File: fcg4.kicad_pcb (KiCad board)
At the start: 2 copper layers, 35 x 35 mm, 34 parts, among them IC1 MP9943AGQ-Z, IC2 MP9943AGQ-Z, J1 USB4105-GF-A-120, J2 SM08B-SRSS-TB, U1 STM32G473CEUx, U2 ICM-42688-P, U4 AP2112K-3.3TRG1, U5 AP2112K-1.8TRG1, Y1 ECS-240-6-37B-7KM-TR

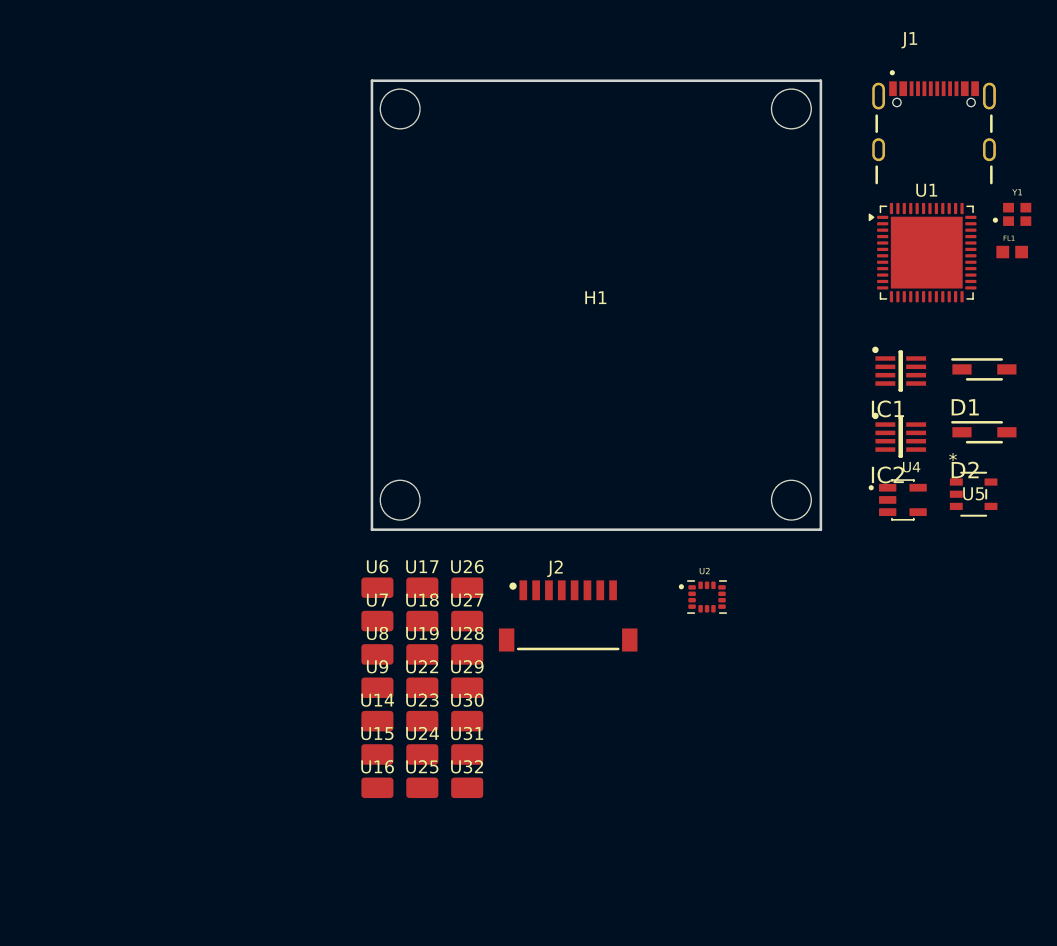
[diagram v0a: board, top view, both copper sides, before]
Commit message: - affected footprints for components - started placing components
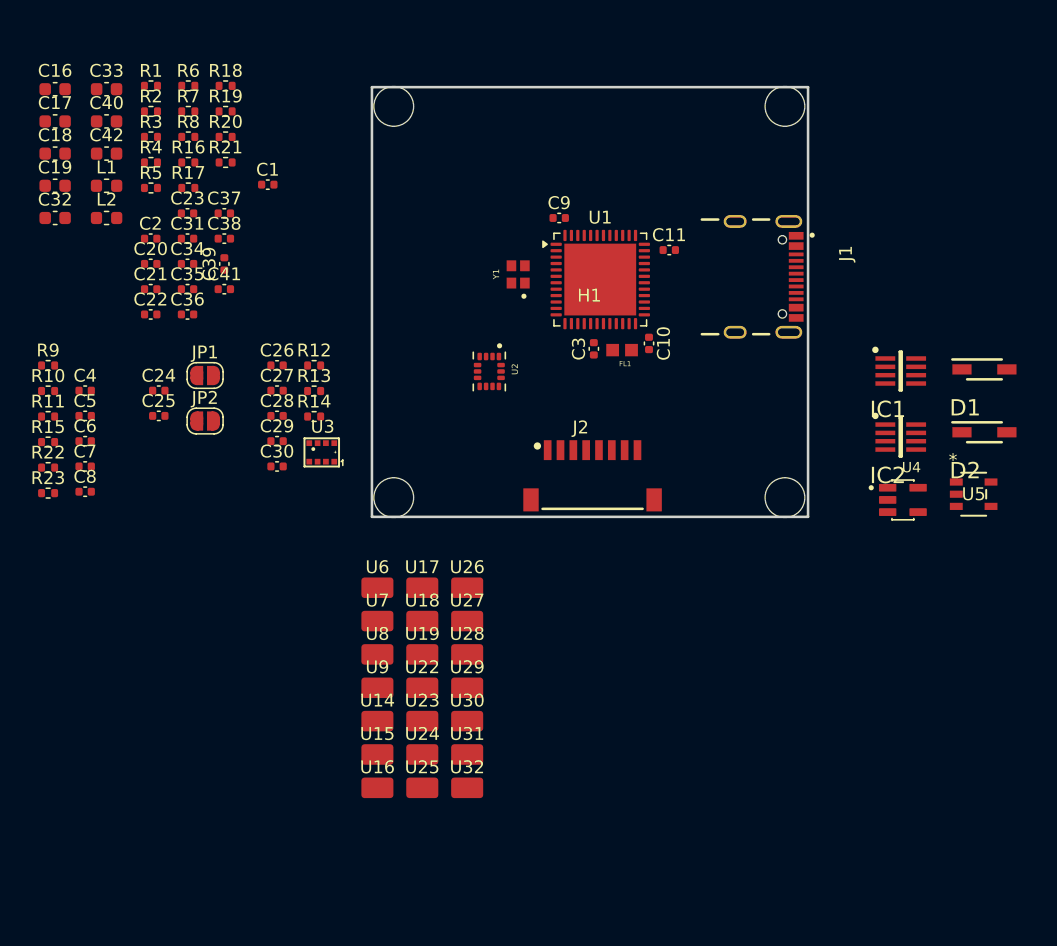
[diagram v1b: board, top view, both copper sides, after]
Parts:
- added C1: 1u, Capacitor_SMD:C_0402_1005Metric, F.Cu at (-8.12, 8.10)
- added C10: 100n, Capacitor_SMD:C_0402_1005Metric, F.Cu at (21.6, 20.5)
- added C11: 100n, Capacitor_SMD:C_0402_1005Metric, F.Cu at (23.2, 13.2)
- added C16: 47u, Capacitor_SMD:C_0603_1608Metric, F.Cu at (-24.7, 0.66)
- added C17: 47u, Capacitor_SMD:C_0603_1608Metric, F.Cu at (-24.7, 3.17)
- added C18: 47u, Capacitor_SMD:C_0603_1608Metric, F.Cu at (-24.7, 5.68)
- added C19: 47u, Capacitor_SMD:C_0603_1608Metric, F.Cu at (-24.7, 8.19)
- added C2: 1u, Capacitor_SMD:C_0402_1005Metric, F.Cu at (-17.2, 12.3)
- added C20: 1u, Capacitor_SMD:C_0402_1005Metric, F.Cu at (-17.2, 14.3)
- added C21: 1u, Capacitor_SMD:C_0402_1005Metric, F.Cu at (-17.2, 16.2)
- added C22: 10u, Capacitor_SMD:C_0402_1005Metric, F.Cu at (-17.2, 18.2)
- added C23: 100n, Capacitor_SMD:C_0402_1005Metric, F.Cu at (-14.4, 10.3)
- added C24: 1u, Capacitor_SMD:C_0402_1005Metric, F.Cu at (-16.6, 24.2)
- added C25: 100n, Capacitor_SMD:C_0402_1005Metric, F.Cu at (-16.6, 26.1)
- added C26: 10n, Capacitor_SMD:C_0402_1005Metric, F.Cu at (-7.40, 22.2)
- added C27: 100n, Capacitor_SMD:C_0402_1005Metric, F.Cu at (-7.40, 24.2)
- added C28: 2.2u, Capacitor_SMD:C_0402_1005Metric, F.Cu at (-7.40, 26.1)
- added C29: 100n, Capacitor_SMD:C_0402_1005Metric, F.Cu at (-7.40, 28.1)
- added C3: 100n, Capacitor_SMD:C_0402_1005Metric, F.Cu at (17.3, 20.9)
- added C30: 100n, Capacitor_SMD:C_0402_1005Metric, F.Cu at (-7.40, 30.1)
- added C31: 100n, Capacitor_SMD:C_0402_1005Metric, F.Cu at (-14.4, 12.3)
- added C32: 22u, Capacitor_SMD:C_0603_1608Metric, F.Cu at (-24.7, 10.7)
- added C33: 22u, Capacitor_SMD:C_0603_1608Metric, F.Cu at (-20.7, 0.66)
- added C34: 10u, Capacitor_SMD:C_0402_1005Metric, F.Cu at (-14.4, 14.3)
- added C35: 1u, Capacitor_SMD:C_0402_1005Metric, F.Cu at (-14.4, 16.2)
- added C36: 100n, Capacitor_SMD:C_0402_1005Metric, F.Cu at (-14.4, 18.2)
- added C37: 100n, Capacitor_SMD:C_0402_1005Metric, F.Cu at (-11.5, 10.3)
- added C38: 10u, Capacitor_SMD:C_0402_1005Metric, F.Cu at (-11.5, 12.3)
- added C39: 10u, Capacitor_SMD:C_0402_1005Metric, F.Cu at (-11.5, 14.3)
- added C4: 1u, Capacitor_SMD:C_0402_1005Metric, F.Cu at (-22.4, 24.2)
- added C40: 22u, Capacitor_SMD:C_0603_1608Metric, F.Cu at (-20.7, 3.17)
- added C41: 1u, Capacitor_SMD:C_0402_1005Metric, F.Cu at (-11.5, 16.2)
- added C42: 22u, Capacitor_SMD:C_0603_1608Metric, F.Cu at (-20.7, 5.68)
- added C5: 8.2p, Capacitor_SMD:C_0402_1005Metric, F.Cu at (-22.4, 26.1)
- added C6: 8.2p, Capacitor_SMD:C_0402_1005Metric, F.Cu at (-22.4, 28.1)
- added C7: 100n, Capacitor_SMD:C_0402_1005Metric, F.Cu at (-22.4, 30.1)
- added C8: 100n, Capacitor_SMD:C_0402_1005Metric, F.Cu at (-22.4, 32.0)
- added C9: 100n, Capacitor_SMD:C_0402_1005Metric, F.Cu at (14.6, 10.7)
- added JP1: SolderJumper_2_Open, Jumper:SolderJumper-2_P1.3mm_Open_RoundedPad1.0x1.5mm, F.Cu at (-13.0, 23.0)
- added JP2: SolderJumper_2_Open, Jumper:SolderJumper-2_P1.3mm_Open_RoundedPad1.0x1.5mm, F.Cu at (-13.0, 26.5)
- added L1: 10uH, Inductor_SMD:L_0603_1608Metric, F.Cu at (-20.7, 8.19)
- added L2: 10uH, Inductor_SMD:L_0603_1608Metric, F.Cu at (-20.7, 10.7)
- added R1: 6.98k, Resistor_SMD:R_0402_1005Metric, F.Cu at (-17.2, 0.40)
- added R10: 5k1, Resistor_SMD:R_0402_1005Metric, F.Cu at (-25.2, 24.2)
- added R11: 5k1, Resistor_SMD:R_0402_1005Metric, F.Cu at (-25.2, 26.2)
- added R12: 10k, Resistor_SMD:R_0402_1005Metric, F.Cu at (-4.51, 22.2)
- added R13: 10k, Resistor_SMD:R_0402_1005Metric, F.Cu at (-4.51, 24.2)
- added R14: 100k, Resistor_SMD:R_0402_1005Metric, F.Cu at (-4.51, 26.2)
- added R15: 10k, Resistor_SMD:R_0402_1005Metric, F.Cu at (-25.2, 28.2)
- added R16: 1M, Resistor_SMD:R_0402_1005Metric, F.Cu at (-14.3, 6.37)
- added R17: 20, Resistor_SMD:R_0402_1005Metric, F.Cu at (-14.3, 8.36)
- added R18: 100k, Resistor_SMD:R_0402_1005Metric, F.Cu at (-11.4, 0.40)
- added R19: 1M, Resistor_SMD:R_0402_1005Metric, F.Cu at (-11.4, 2.39)
- added R2: 41.2k, Resistor_SMD:R_0402_1005Metric, F.Cu at (-17.2, 2.39)
- added R20: 100k, Resistor_SMD:R_0402_1005Metric, F.Cu at (-11.4, 4.38)
- added R21: 20, Resistor_SMD:R_0402_1005Metric, F.Cu at (-11.4, 6.37)
- added R22: 10k, Resistor_SMD:R_0402_1005Metric, F.Cu at (-25.2, 30.2)
- added R23: 10k, Resistor_SMD:R_0402_1005Metric, F.Cu at (-25.2, 32.1)
- added R3: 51k, Resistor_SMD:R_0402_1005Metric, F.Cu at (-17.2, 4.38)
- added R4: 51k, Resistor_SMD:R_0402_1005Metric, F.Cu at (-17.2, 6.37)
- added R5: 3.92k, Resistor_SMD:R_0402_1005Metric, F.Cu at (-17.2, 8.36)
- added R6: 41.2k, Resistor_SMD:R_0402_1005Metric, F.Cu at (-14.3, 0.40)
- added R7: 10k, Resistor_SMD:R_0402_1005Metric, F.Cu at (-14.3, 2.39)
- added R8: 1k, Resistor_SMD:R_0402_1005Metric, F.Cu at (-14.3, 4.38)
- added R9: 250, Resistor_SMD:R_0402_1005Metric, F.Cu at (-25.2, 22.2)
- added U3: ~, fcg4_fp:SENSOR-SMD_SPL06-001, F.Cu at (-3.91, 29.0)
- moved Y1 39.2 mm to (11.4, 15.1), turned to 90 degrees
- moved FL1 31.4 mm to (19.5, 21.0), turned to 180 degrees
- moved U1 25.5 mm to (17.8, 15.5)
- moved U2 24.4 mm to (9.15, 22.7), turned to -90 degrees
- moved J1 18.4 mm to (28.3, 15.3), turned to -90 degrees
- moved J2 11.1 mm to (17.2, 33.6)
- moved H1 0.54 mm to (16.9, 17.2)
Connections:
- net Net-(U1-PF0) renamed /MCU/OSC_IN
- net Net-(U1-PF1) renamed /MCU/OSC_OUT
- U26 pad 1: I2C1_SCL_ -> I2C1_SCL
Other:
- board size 35 x 35 mm -> 34 x 33.5 mm
- copper layers 2 -> 4

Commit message: Placed every components on one face only
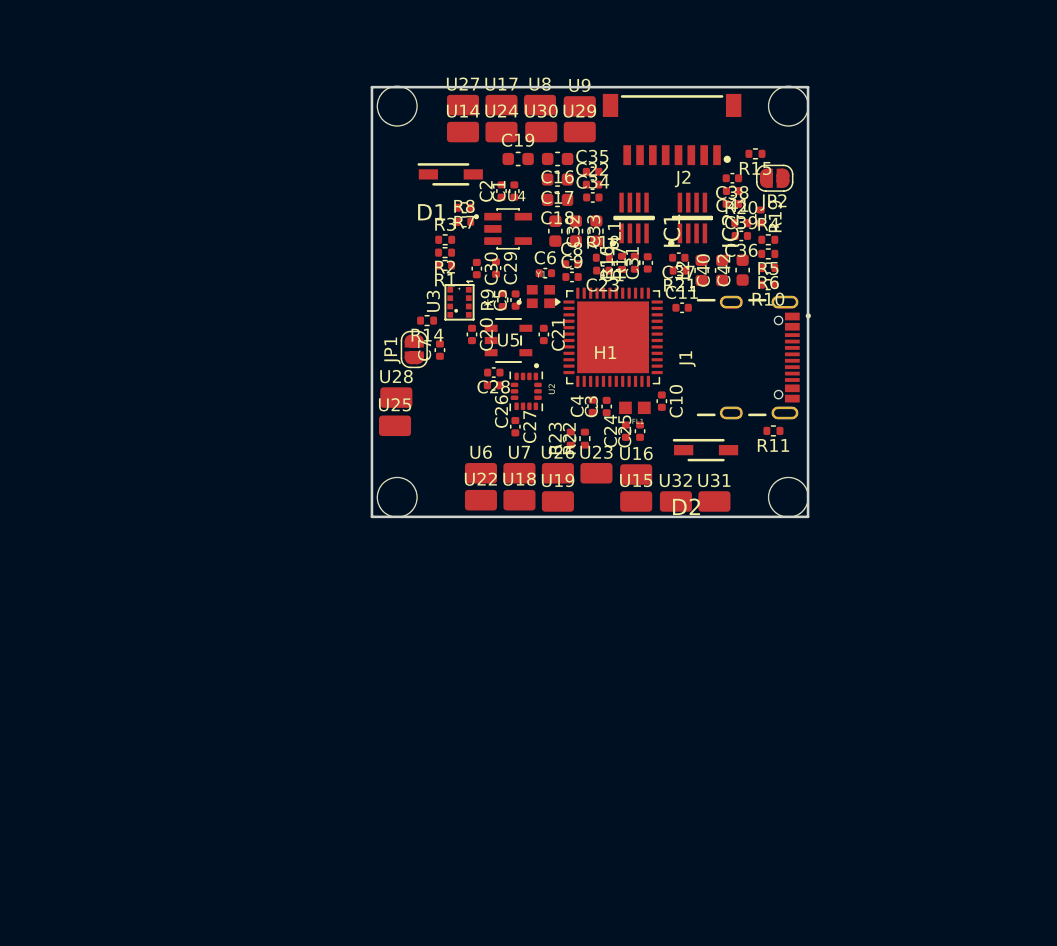
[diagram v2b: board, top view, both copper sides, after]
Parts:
- removed R12, R13: 10k, Resistor_SMD:R_0402_1005Metric
- moved R15 59.5 mm to (29.9, 5.70), turned to 180 degrees
- moved R10 56.7 mm to (30.9, 15.9), turned to 180 degrees
- moved R11 56.6 mm to (31.3, 27.3), turned to 180 degrees
- moved C42 50.4 mm to (28.9, 14.8), turned to 90 degrees
- moved C40 49.4 mm to (27.3, 14.8), turned to 90 degrees
- moved U24 48.9 mm to (10.1, 4.00)
- moved R4 48.5 mm to (30.9, 12.4)
- moved R5 48.4 mm to (30.9, 13.5), turned to 180 degrees
- moved JP2 48.3 mm to (31.4, 7.60), turned to 180 degrees
- moved U9 48.0 mm to (16.2, 2.00)
- moved R6 47.4 mm to (30.9, 14.6), turned to 180 degrees
- moved L2 46.6 mm to (25.7, 14.8), turned to 90 degrees
- moved U14 46.4 mm to (7.10, 4.00)
- moved U30 46.3 mm to (13.2, 4.00)
- moved U8 44.7 mm to (13.1, 1.90)
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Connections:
- net Net-(C5-Pad1) renamed /MCU/RC_OSC
- net Net-(U3-SDO) renamed /Sensor/SD0
- net Net-(U5-VOUT) renamed /Power/VOUT

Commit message: Started routing
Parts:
- moved U15 33.0 mm to (9.80, 1.60)
- moved U27 30.8 mm to (7.20, 32.7)
- moved U16 29.5 mm to (15.6, 1.60)
- moved U9 29.2 mm to (21.7, 30.7)
- moved U29 28.9 mm to (13.0, 32.7)
- moved U30 28.8 mm to (15.9, 32.7)
- moved U8 28.8 mm to (13.0, 30.7)
- moved U24 23.6 mm to (1.60, 26.0)
- moved U19 23.1 mm to (1.50, 13.7), turned to 90 degrees
- moved U28 21.4 mm to (21.7, 32.7)
- moved U18 19.0 mm to (1.50, 16.6), turned to 90 degrees
- moved U32 13.6 mm to (10.1, 32.7)
- moved U22 11.1 mm to (1.60, 24.0)
- moved U31 7.90 mm to (18.8, 32.7)
- moved U26 4.30 mm to (18.8, 30.7)
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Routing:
- net RX3: track 0.00 -> 58.5 mm, vias 0 -> 3
- net TX3: track 0.00 -> 31.7 mm, vias 0 -> 2
- net RX4: track 0.00 -> 28.4 mm, vias 0 -> 3
- net I2C1_SDA: track 0.00 -> 28.4 mm, vias 0 -> 3
- net MOTOR2: track 0.00 -> 27.5 mm, vias 0 -> 2
- net TX1: track 0.00 -> 26.7 mm, vias 0 -> 2
- net BEEPER: track 0.00 -> 23.9 mm, vias 0 -> 2
- net TX4: track 0.00 -> 23.4 mm, vias 0 -> 3
- net RX1: track 0.00 -> 22.5 mm, vias 0 -> 2
- net CURRENT_SENSOR: track 0.00 -> 20.4 mm, vias 0 -> 2
- net RX2: track 0.00 -> 20.2 mm, vias 0 -> 2
- net I2C1_SCL: track 0.00 -> 19.8 mm, vias 0 -> 2
- net MOTOR1: track 0.00 -> 18.2 mm, vias 0 -> 2
- net VOLTAGE_SENSOR: track 0.00 -> 18.2 mm
- net MOTOR3: track 0.00 -> 15.3 mm
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
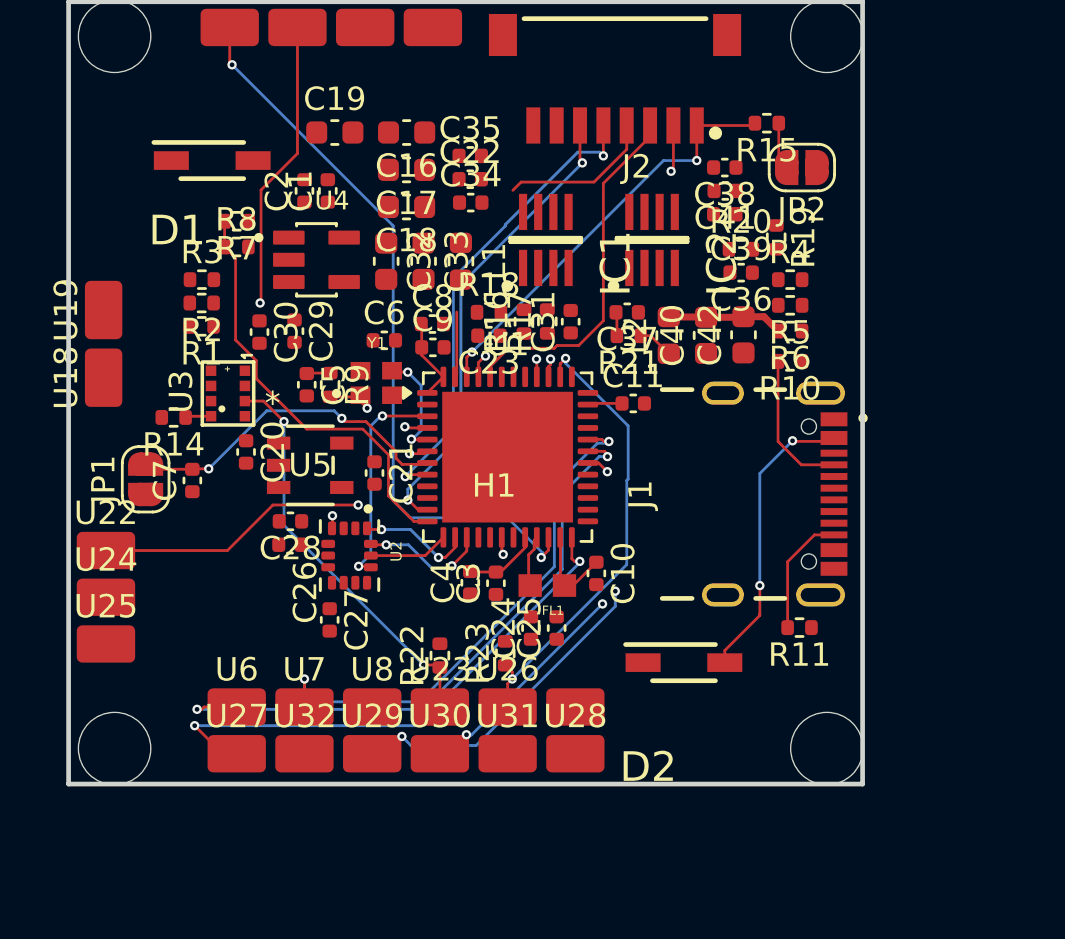
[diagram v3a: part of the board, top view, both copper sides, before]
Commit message: removed schottky diodes to use ideal diodes smaller
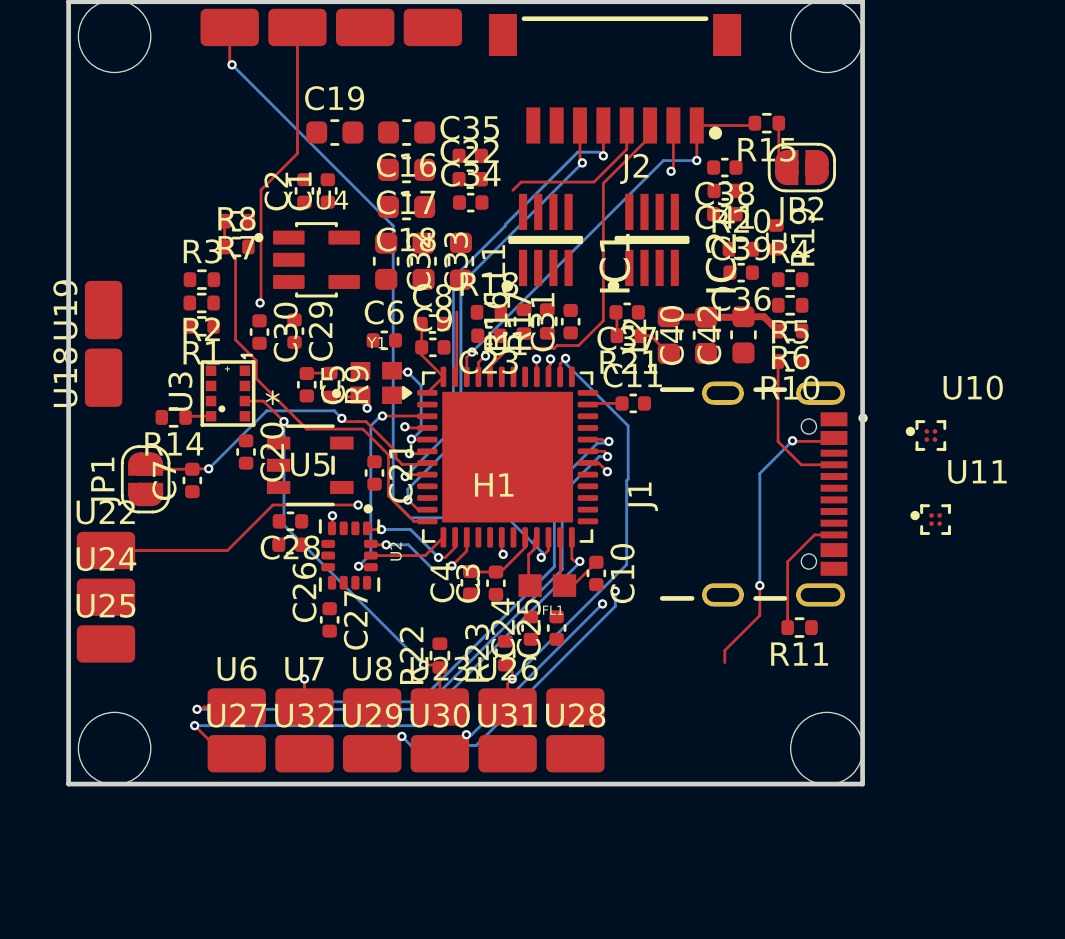
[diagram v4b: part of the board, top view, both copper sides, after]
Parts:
- removed D1, D2: 1N5819HW-7-F, fcg4_fp:SOD3716X145M
- added U10: MAX40200ANS_T, fcg4_fp:BGA4N35P2X2_72X72X50N, F.Cu at (36.9, 19.1)
- added U11: MAX40200ANS_T, fcg4_fp:BGA4N35P2X2_72X72X50N, F.Cu at (37.1, 22.7)
